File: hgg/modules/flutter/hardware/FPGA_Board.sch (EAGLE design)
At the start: 85 parts, among them IC1 AT45DB161D-SU, IC2 MEGA8-AI, IC3 MAX481CSA, Q1 8Mhz, U2 XC3S50AVQ100, X1 BU-SMA-V, X2 MINI-USB-32005-201

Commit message: changed package of resistors and capasitors to 0603 added values
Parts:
- C1, C2, C3, C4, C5, C6: value (none) -> 100n; device resistor:C-EUC0805 -> resistor:C-EUC0603
- C10, C7, C8, C9: value (none) -> 10u; device resistor:CPOL-EU085CS-1AR -> resistor:C-EUC0603
- C11, C12: device resistor:C-EUC0805 -> resistor:C-EUC0603
- C13, C14, C15, C16, C18, C19, C20, C21, C22, C23, C24: value (none) -> 100n
- C17, C25: value (none) -> 15p
- R1, R13, R14, R15, R18, R19, R2, R20, R3, R4, R5, R6, R7, R8: device resistor:R-EU_M0805 -> resistor:R-EU_R0603
- R10, R11, R9: value (none) -> 68; device resistor:R-EU_M0805 -> resistor:R-EU_R0603
- R12: value (none) -> 4.7k; device resistor:R-EU_M0805 -> resistor:R-EU_R0603
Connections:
- net +5V: now also C10.1; no longer C10.+
- net GND: now also C10.2, C7.2, C8.2, C9.2; no longer C10.-, C7.-, C8.-, C9.-
- net VCC1.2: now also C9.1; no longer C9.+
- net VCC2.5: now also C8.1; no longer C8.+
- net VCC3.3: now also C7.1; no longer C7.+

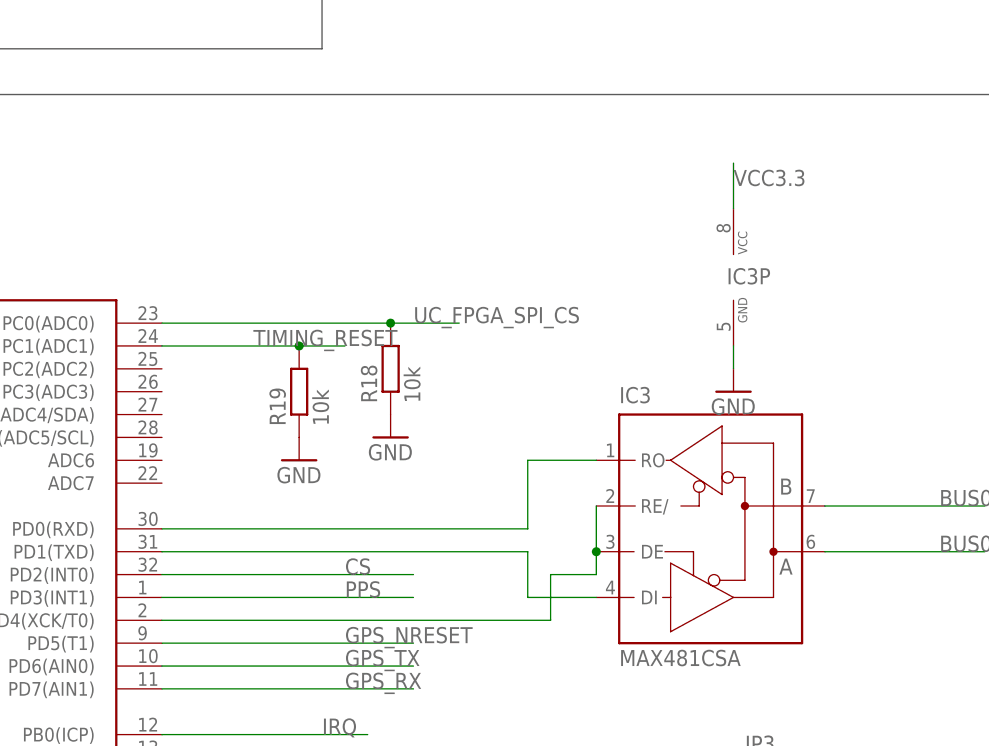
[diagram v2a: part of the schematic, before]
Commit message: changed supply of rs485 transciever to 5V
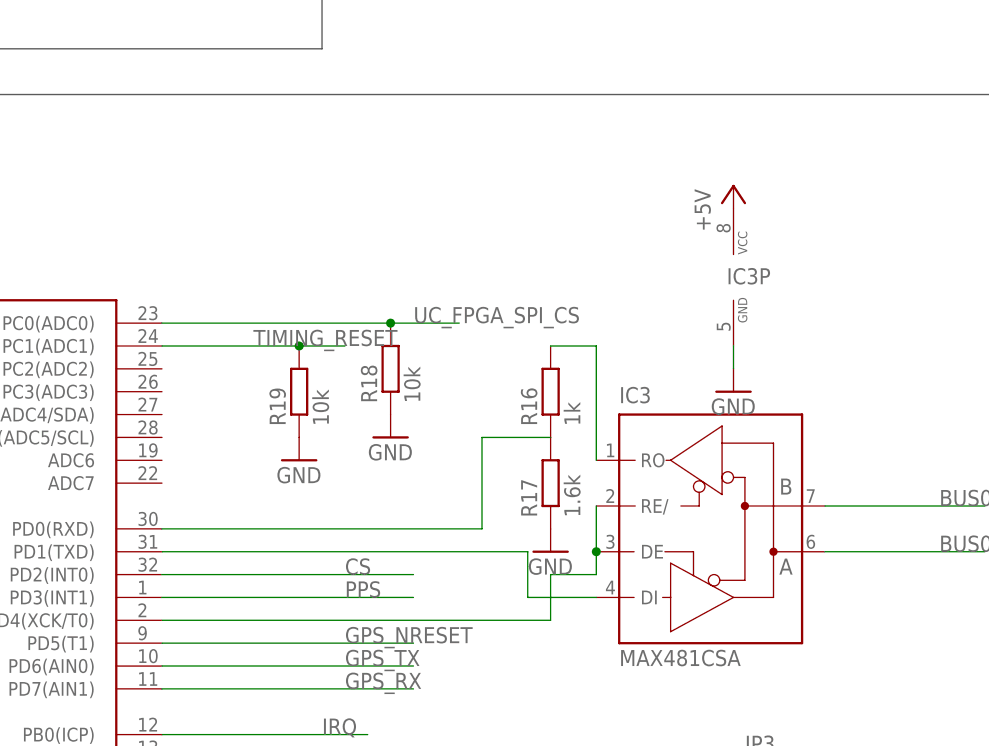
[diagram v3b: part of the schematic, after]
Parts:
- added R16: 1k, resistor:R-EU_R0603
- added R17: 1.6k, resistor:R-EU_R0603
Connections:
- removed net DO: IC2.PD0(RXD), IC3G$1.RO
- new net N$6: IC2.PD0(RXD), R16.1, R17.2
- new net N$9: IC3G$1.RO, R16.2
- net +5V: now also IC3P.VCC
- net GND: now also R17.1
- net VCC3.3: no longer IC3P.VCC
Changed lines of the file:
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@@
 <part name="GND50" library="supply1" deviceset="GND" device=""/>
 <part name="GND51" library="supply1" deviceset="GND" device=""/>
+<part name="R16" library="resistor" deviceset="R-EU_" device="R0603" value="1k"/>
+<part name="R17" library="resistor" deviceset="R-EU_" device="R0603" value="1.6k"/>
+<part name="GND52" library="supply1" deviceset="GND" device=""/>
+<part name="P+8" library="supply1" deviceset="+5V" device=""/>
 </parts>
 <sheets>
@@
 <instance part="GND50" gate="1" x="106.68" y="198.12"/>
 <instance part="GND51" gate="1" x="109.22" y="322.58"/>
+<instance part="R16" gate="G$1" x="469.9" y="198.12" rot="R90"/>
+<instance part="R17" gate="G$1" x="469.9" y="187.96" rot="R90"/>
+<instance part="GND52" gate="1" x="469.9" y="180.34"/>
+<instance part="P+8" gate="1" x="490.22" y="220.98"/>
 </instances>
 <busses>
@@
 <pinref part="GND51" gate="1" pin="GND"/>
 </segment>
+<segment>
+<pinref part="R17" gate="G$1" pin="1"/>
+<pinref part="GND52" gate="1" pin="GND"/>
+</segment>
 </net>
 <net name="+5V" class="0">
@@
 <wire x1="132.08" y1="342.9" x2="132.08" y2="320.04" width="0.1524" layer="91"/>
 <label x="132.08" y="320.04" size="1.778" layer="95" rot="R90"/>
+</segment>
+<segment>
+<pinref part="IC3" gate="P" pin="VCC"/>
+<pinref part="P+8" gate="1" pin="+5V"/>
 </segment>
 </net>
@@
 <wire x1="335.28" y1="281.94" x2="335.28" y2="297.18" width="0.1524" layer="91"/>
 <junction x="335.28" y="297.18"/>
-</segment>
-<segment>
-<wire x1="490.22" y1="223.52" x2="490.22" y2="218.44" width="0.1524" layer="91"/>
-<pinref part="IC3" gate="P" pin="VCC"/>
-<label x="490.22" y="220.98" size="1.778" layer="95"/>
 </segment>
 <segment>
@@
 </segment>
 </net>
-<net name="DO" class="0">
-<segment>
-<pinref part="IC2" gate="G$1" pin="PD0(RXD)"/>
-<wire x1="426.72" y1="182.88" x2="467.36" y2="182.88" width="0.1524" layer="91"/>
-<pinref part="IC3" gate="G$1" pin="RO"/>
-<wire x1="467.36" y1="190.5" x2="474.98" y2="190.5" width="0.1524" layer="91"/>
-<wire x1="467.36" y1="182.88" x2="467.36" y2="190.5" width="0.1524" layer="91"/>
-</segment>
-</net>
 <net name="BUS1-" class="0">
 <segment>
@@
 </segment>
 </net>
+<net name="N$6" class="0">
+<segment>
+<pinref part="R17" gate="G$1" pin="2"/>
+<pinref part="R16" gate="G$1" pin="1"/>
+<wire x1="469.9" y1="193.04" x2="462.28" y2="193.04" width="0.1524" layer="91"/>
+<wire x1="462.28" y1="193.04" x2="462.28" y2="182.88" width="0.1524" layer="91"/>
+<pinref part="IC2" gate="G$1" pin="PD0(RXD)"/>
+<wire x1="462.28" y1="182.88" x2="426.72" y2="182.88" width="0.1524" layer="91"/>
+</segment>
+</net>
+<net name="N$9" class="0">
+<segment>
+<pinref part="IC3" gate="G$1" pin="RO"/>
+<wire x1="474.98" y1="190.5" x2="474.98" y2="203.2" width="0.1524" layer="91"/>
+<pinref part="R16" gate="G$1" pin="2"/>
+<wire x1="474.98" y1="203.2" x2="469.9" y2="203.2" width="0.1524" layer="91"/>
+</segment>
+</net>

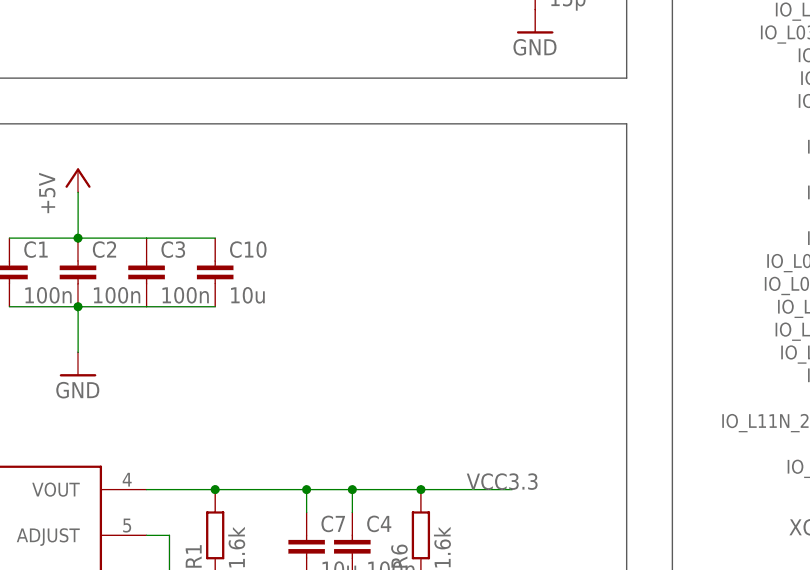
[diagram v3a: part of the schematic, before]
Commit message: flutter pcb is ready for review
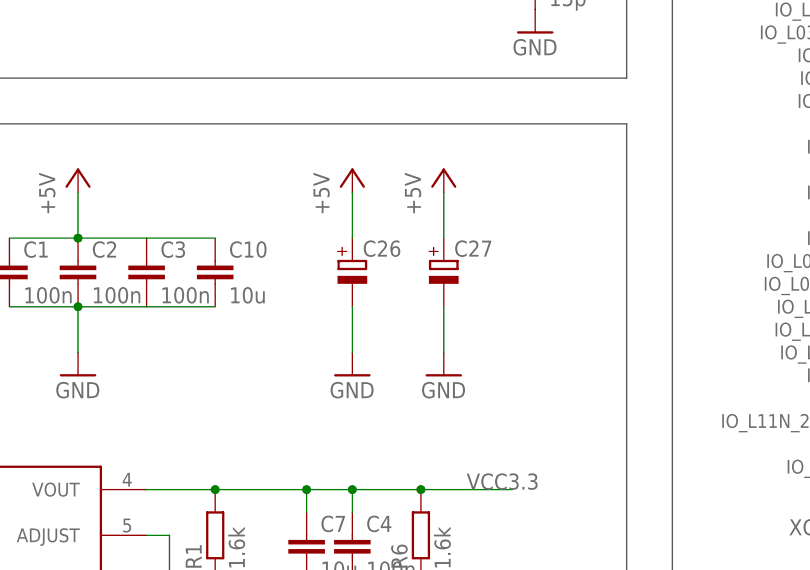
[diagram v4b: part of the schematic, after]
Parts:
- added C26, C27: (no value), resistor:CPOL-EUE5-8.5
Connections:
- net +5V: now also C26.+, C27.+
- net GND: now also C26.-, C27.-
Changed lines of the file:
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@@
 <part name="GND52" library="supply1" deviceset="GND" device=""/>
 <part name="P+8" library="supply1" deviceset="+5V" device=""/>
+<part name="C26" library="resistor" deviceset="CPOL-EU" device="E5-8.5"/>
+<part name="C27" library="resistor" deviceset="CPOL-EU" device="E5-8.5"/>
+<part name="P+10" library="supply1" deviceset="+5V" device=""/>
+<part name="P+11" library="supply1" deviceset="+5V" device=""/>
+<part name="GND53" library="supply1" deviceset="GND" device=""/>
+<part name="GND54" library="supply1" deviceset="GND" device=""/>
 </parts>
 <sheets>
@@
 <instance part="GND52" gate="1" x="469.9" y="180.34"/>
 <instance part="P+8" gate="1" x="490.22" y="220.98"/>
+<instance part="C26" gate="G$1" x="86.36" y="172.72"/>
+<instance part="C27" gate="G$1" x="96.52" y="172.72"/>
+<instance part="P+10" gate="1" x="86.36" y="182.88"/>
+<instance part="P+11" gate="1" x="96.52" y="182.88"/>
+<instance part="GND53" gate="1" x="86.36" y="160.02"/>
+<instance part="GND54" gate="1" x="96.52" y="160.02"/>
 </instances>
 <busses>
@@
 <pinref part="GND52" gate="1" pin="GND"/>
 </segment>
+<segment>
+<pinref part="GND53" gate="1" pin="GND"/>
+<pinref part="C26" gate="G$1" pin="-"/>
+<wire x1="86.36" y1="162.56" x2="86.36" y2="167.64" width="0.1524" layer="91"/>
+</segment>
+<segment>
+<pinref part="C27" gate="G$1" pin="-"/>
+<pinref part="GND54" gate="1" pin="GND"/>
+<wire x1="96.52" y1="167.64" x2="96.52" y2="162.56" width="0.1524" layer="91"/>
+</segment>
 </net>
 <net name="+5V" class="0">
@@
 <pinref part="P+8" gate="1" pin="+5V"/>
 </segment>
+<segment>
+<pinref part="P+11" gate="1" pin="+5V"/>
+<pinref part="C27" gate="G$1" pin="+"/>
+<wire x1="96.52" y1="180.34" x2="96.52" y2="175.26" width="0.1524" layer="91"/>
+</segment>
+<segment>
+<pinref part="P+10" gate="1" pin="+5V"/>
+<pinref part="C26" gate="G$1" pin="+"/>
+<wire x1="86.36" y1="180.34" x2="86.36" y2="175.26" width="0.1524" layer="91"/>
+</segment>
 </net>

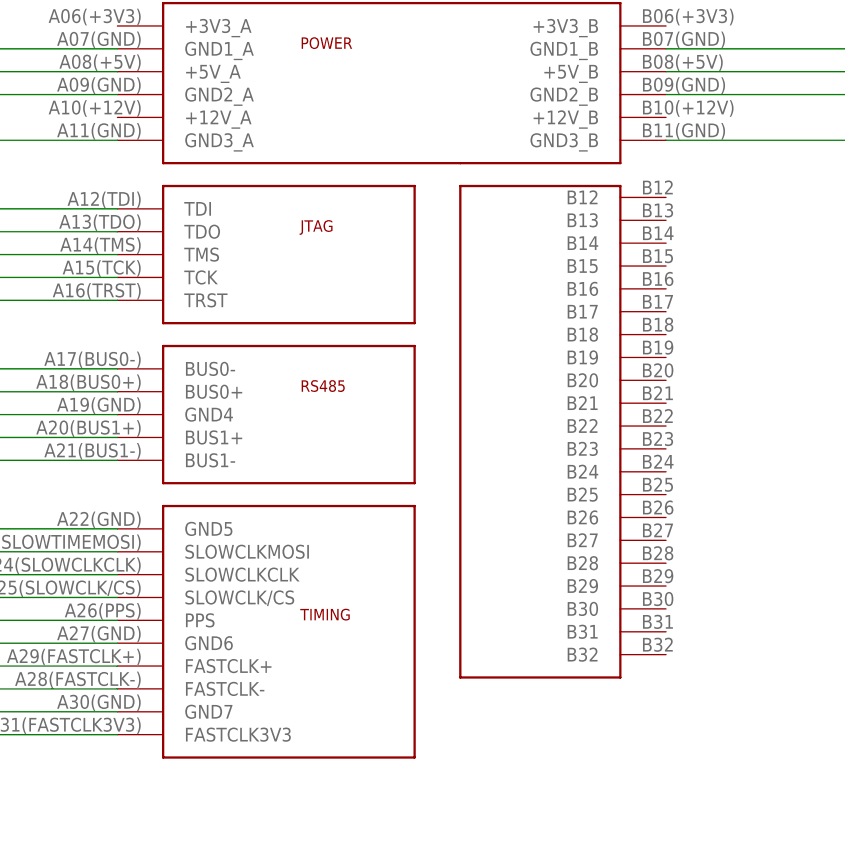
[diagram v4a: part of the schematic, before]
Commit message: - 0mil thermal isolation space between cooling pads and ground plane - deleted one misrouted signal path - added info text to layout
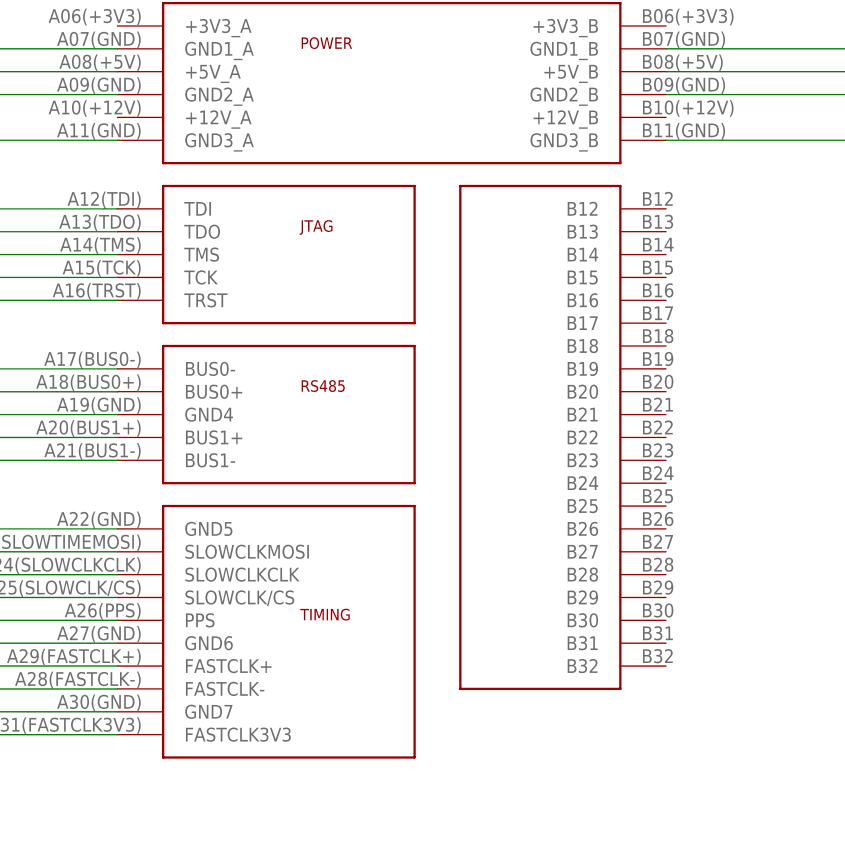
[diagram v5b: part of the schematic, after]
